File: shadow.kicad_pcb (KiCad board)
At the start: 2 copper layers, 69.8 x 78.7 mm, 100 parts, among them IC2 XB8089D, J1 USB_C_Receptacle, SW1 SW_Push, SW2 SW_Push, SW3 SW_SPST, U1 TCA9548APWR, U2 TCA9548APWR, U3 BQ24092DGQR, U4 TPS61085DGKR, U5 TPS259621DDAT

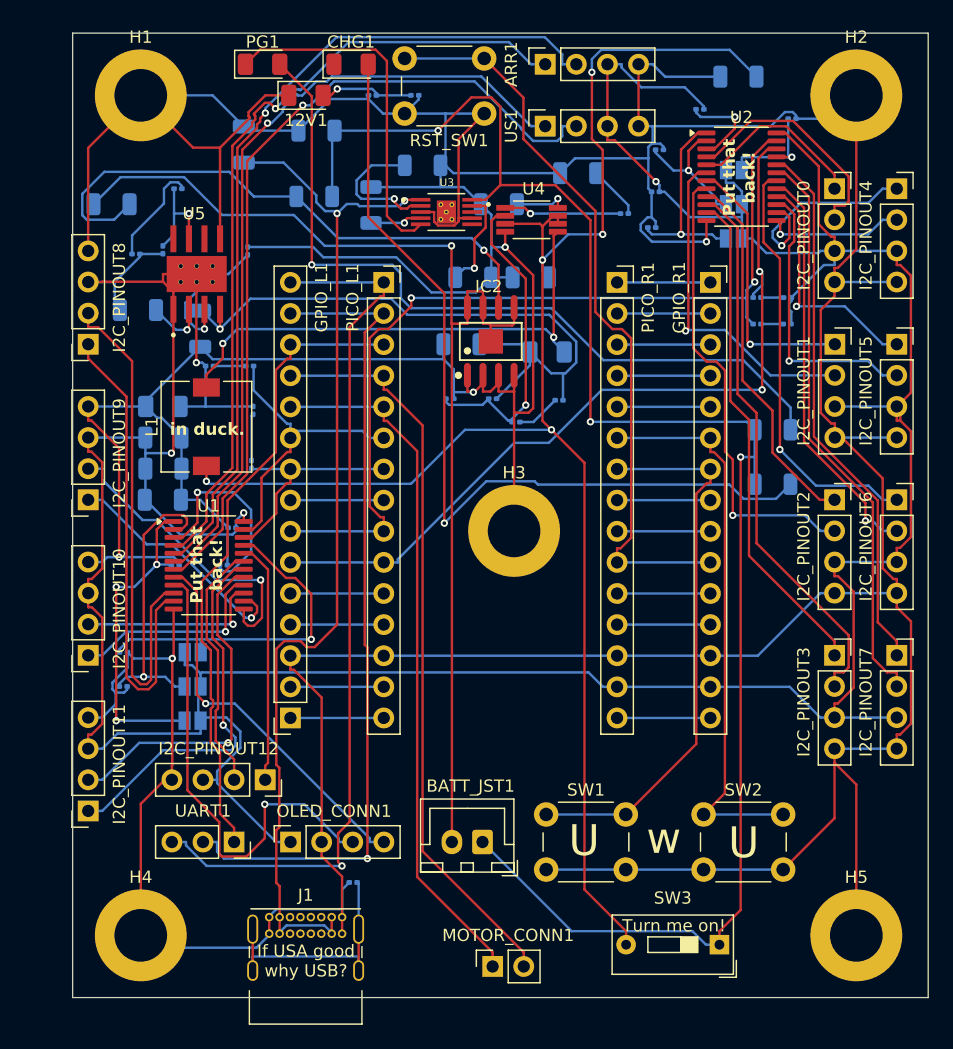
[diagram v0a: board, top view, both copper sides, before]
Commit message: Update to new cap footprint
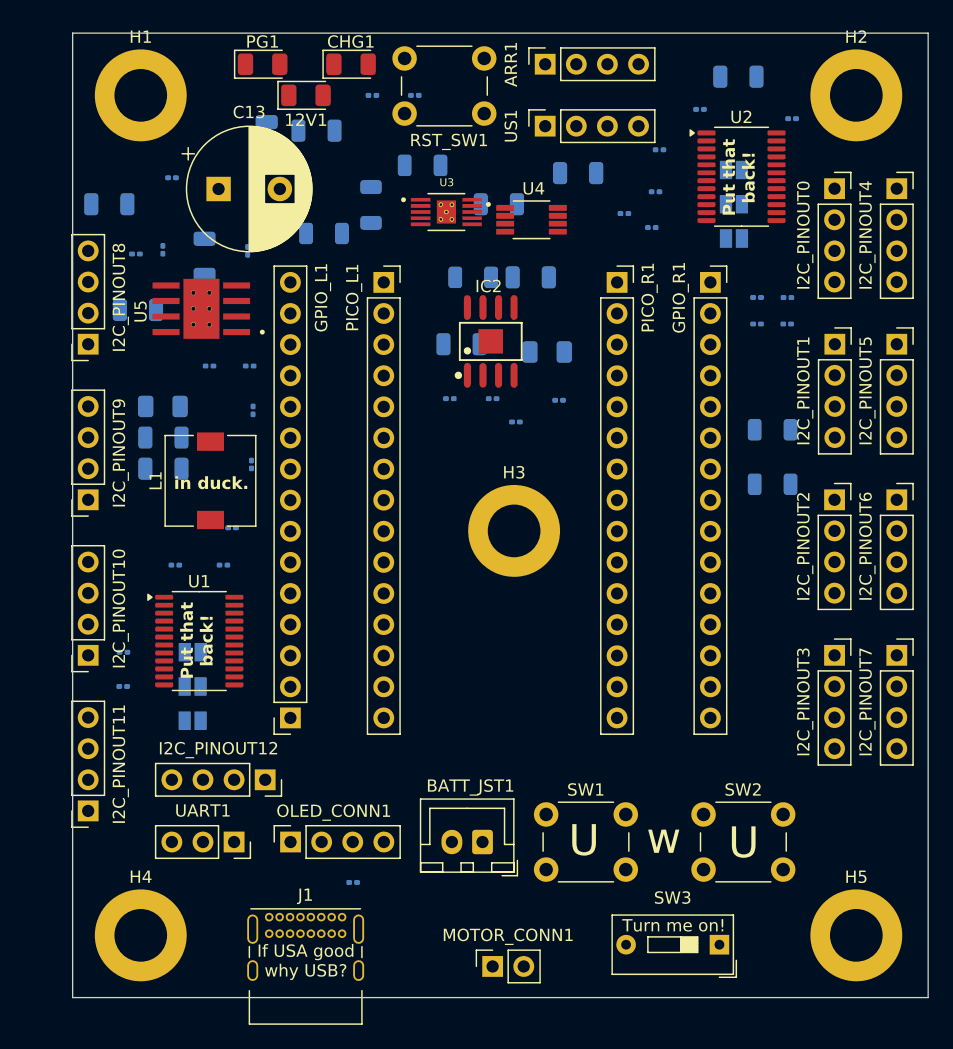
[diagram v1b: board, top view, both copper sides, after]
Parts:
- C13: footprint Capacitor_SMD:C_1206_3216Metric -> Capacitor_THT:CP_Radial_D10.0mm_P5.00mm; moved to F.Cu
- moved C13 25.8 mm to (110.5, 61.0), turned to 0 degrees
- moved U1 6.23 mm to (108.9, 97.9)
- moved C3 5.88 mm to (109.3, 66.5), turned to 90 degrees
- moved L1 4.43 mm to (109.8, 84.8)
- moved R5 3.13 mm to (119.1, 64.6)
- moved U5 2.86 mm to (109.1, 70.8), turned to 180 degrees
- moved C8 1.90 mm to (114.4, 57.0)
- moved R17 1.01 mm to (106.7, 60.1)
- moved C7 0.18 mm to (101.6, 62.2)
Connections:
- C10 pad 2: VCC -> GND
- C11 pad 1: GND -> VCC
- C11 pad 2: VCC -> GND
- C12 pad 1: GND -> VCC
- C12 pad 2: VCC -> GND
- C13 pad 1: GND -> VCC
- C13 pad 2: VCC -> GND
- D2 pad 1: GND -> VCC
- D2 pad 2: VCC -> GND
- R12 pad 1: VCC -> GND
- R13 pad 1: VCC -> GND
- R14 pad 2: GND -> VCC
- U5 pad 1: VCC -> GND
- U5 pad 5: GND -> VCC
- U5 pad 9: VCC -> GND
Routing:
- net GND: track 572.3 -> 0.00 mm, vias 5 -> 0
- net VCC: track 321.5 -> 0.00 mm, vias 4 -> 0
- net /battery/BAT+: track 137.3 -> 0.00 mm, vias 3 -> 0
- net Net-(SW3-B): track 134.9 -> 0.00 mm, vias 5 -> 0
- net /battery/BAT-: track 94.3 -> 0.00 mm, vias 1 -> 0
- net Net-(U3-IN): track 86.7 -> 0.00 mm, vias 2 -> 0
- net /GPIO8: track 73.3 -> 0.00 mm, vias 2 -> 0
- net /GPIO0: track 72.0 -> 0.00 mm, vias 1 -> 0
- net Net-(CHG1-A): track 70.8 -> 0.00 mm, vias 1 -> 0
- net /SENSOR_SCL: track 69.0 -> 0.00 mm, vias 1 -> 0
- net /US_SCL: track 68.9 -> 0.00 mm, vias 1 -> 0
- net /GPIO9: track 67.8 -> 0.00 mm, vias 2 -> 0
- net /GPIO1: track 67.3 -> 0.00 mm, vias 1 -> 0
- net /SENSOR_SDA: track 65.8 -> 0.00 mm, vias 1 -> 0
- net /US_SDA: track 65.5 -> 0.00 mm, vias 1 -> 0
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
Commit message: route traces
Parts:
- moved J1 0.94 mm to (114.6, 119.5)
- moved R30 0.77 mm to (121.6, 116.8)
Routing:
- net GND: track 0.00 -> 570.2 mm, vias 0 -> 4
- net VCC: track 0.00 -> 351.8 mm, vias 0 -> 4
- net /battery/BAT+: track 0.00 -> 138.4 mm, vias 0 -> 5
- net Net-(SW3-B): track 0.00 -> 126.4 mm, vias 0 -> 5
- net /battery/BAT-: track 0.00 -> 89.2 mm, vias 0 -> 1
- net Net-(U3-IN): track 0.00 -> 85.8 mm, vias 0 -> 2
- net /US_SCL: track 0.00 -> 82.4 mm, vias 0 -> 1
- net /SENSOR_SCL: track 0.00 -> 80.7 mm, vias 0 -> 1
- net /GPIO9: track 0.00 -> 79.0 mm, vias 0 -> 2
- net /GPIO8: track 0.00 -> 78.9 mm, vias 0 -> 2
- net /US_SDA: track 0.00 -> 78.5 mm, vias 0 -> 1
- net /SENSOR_SDA: track 0.00 -> 74.1 mm, vias 0 -> 1
- net /GPIO1: track 0.00 -> 71.4 mm, vias 0 -> 1
- net Net-(PG1-A): track 0.00 -> 70.4 mm, vias 0 -> 1
- net Net-(CHG1-A): track 0.00 -> 65.0 mm, vias 0 -> 1
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
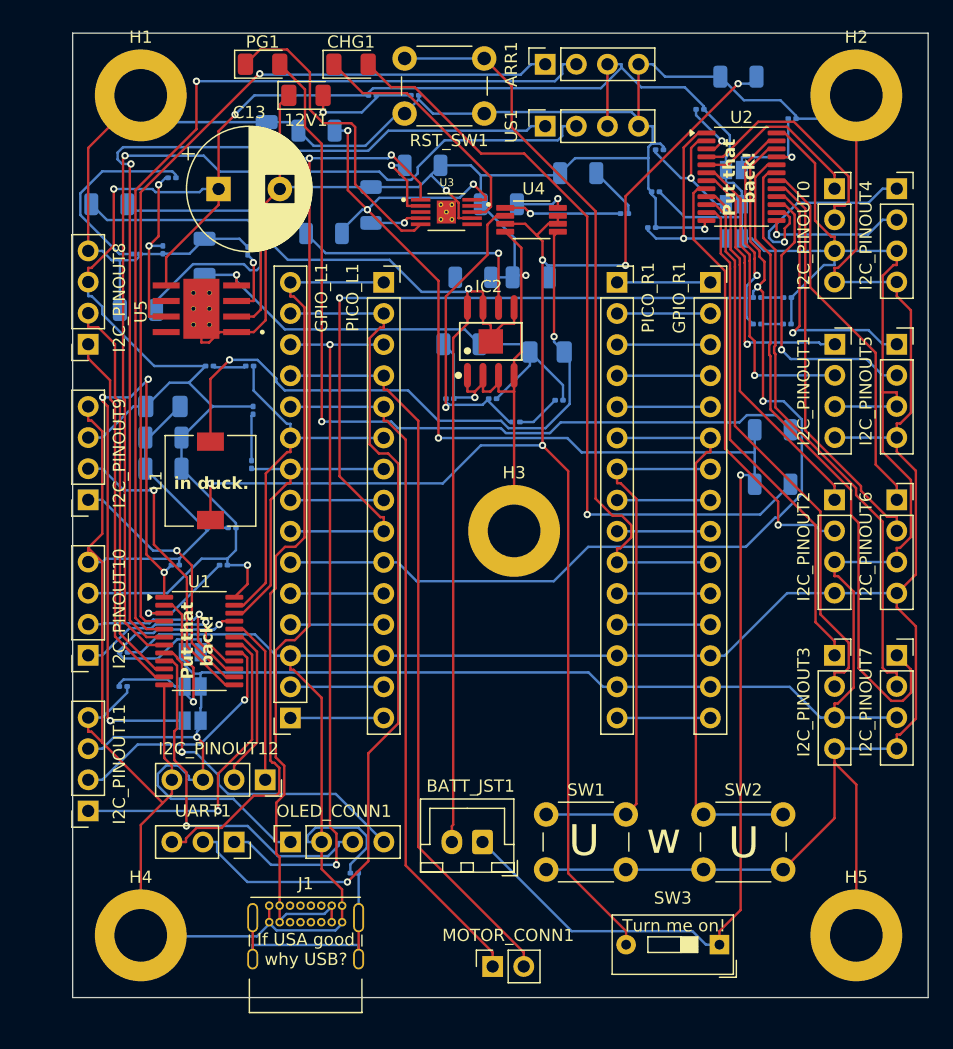
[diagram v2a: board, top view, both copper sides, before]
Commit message: fix pico mount width and orientation of left gpio
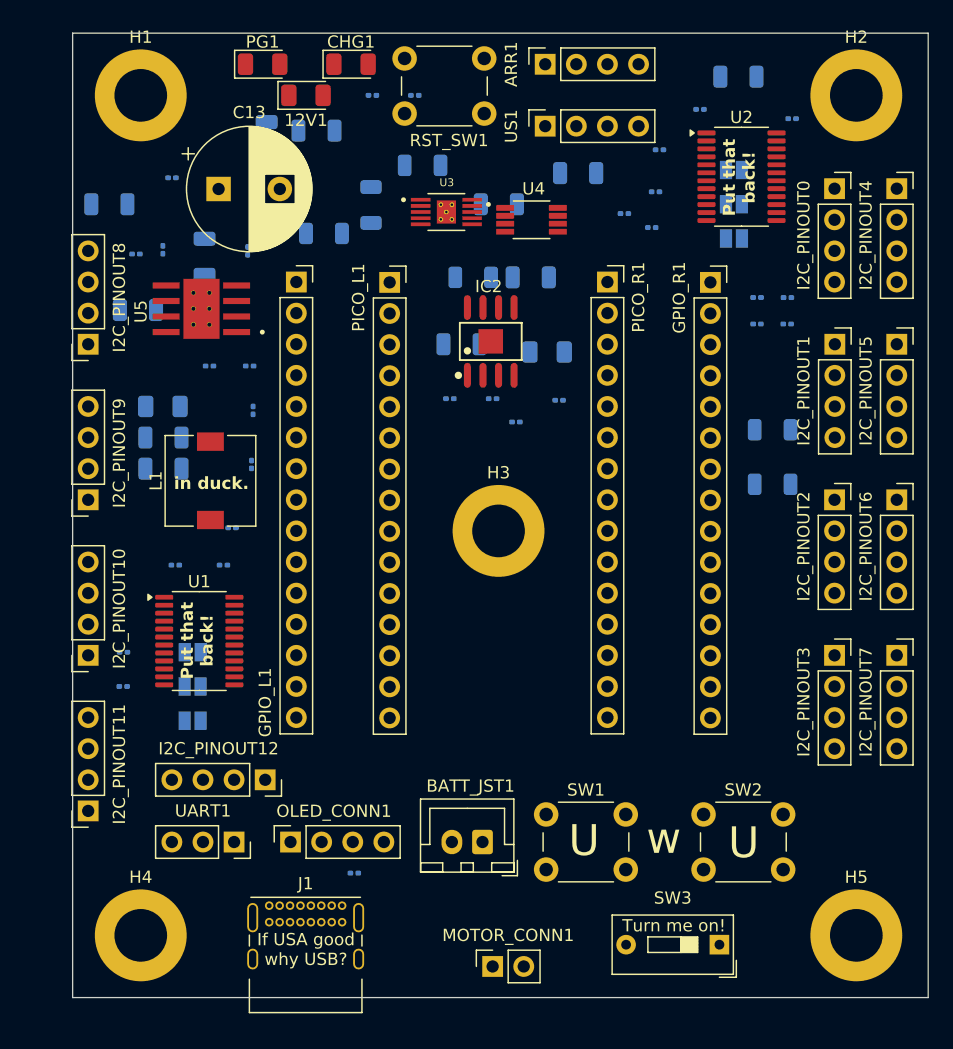
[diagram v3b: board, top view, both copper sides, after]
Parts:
- moved GPIO_L1 35.6 mm to (116.8, 68.6), turned to 0 degrees
- moved H3 1.27 mm to (133.3, 88.9)
- moved PICO_R1 0.79 mm to (142.2, 68.6)
- moved PICO_L1 0.48 mm to (124.5, 68.6)
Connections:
- GPIO_L1 pad 1: /GPIO14 -> /GPIO0
- GPIO_L1 pad 10: /GPIO5 -> /GPIO9
- GPIO_L1 pad 11: /GPIO4 -> /GPIO10
- GPIO_L1 pad 12: /GPIO3 -> /GPIO11
- GPIO_L1 pad 13: /GPIO2 -> GND
- GPIO_L1 pad 14: /GPIO1 -> /GPIO13
- GPIO_L1 pad 15: /GPIO0 -> /GPIO14
- GPIO_L1 pad 2: /GPIO13 -> /GPIO1
- GPIO_L1 pad 3: GND -> /GPIO2
- GPIO_L1 pad 4: /GPIO11 -> /GPIO3
- GPIO_L1 pad 5: /GPIO10 -> /GPIO4
- GPIO_L1 pad 6: /GPIO9 -> /GPIO5
- GPIO_L1 pad 7: /GPIO8 -> /GPIO6
- GPIO_L1 pad 9: /GPIO6 -> /GPIO8
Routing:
- net GND: track 570.2 -> 0.00 mm, vias 4 -> 0
- net VCC: track 351.8 -> 0.00 mm, vias 4 -> 0
- net /battery/BAT+: track 138.4 -> 0.00 mm, vias 5 -> 0
- net Net-(SW3-B): track 126.4 -> 0.00 mm, vias 5 -> 0
- net /battery/BAT-: track 89.2 -> 0.00 mm, vias 1 -> 0
- net Net-(U3-IN): track 85.8 -> 0.00 mm, vias 2 -> 0
- net /US_SCL: track 82.4 -> 0.00 mm, vias 1 -> 0
- net /SENSOR_SCL: track 80.7 -> 0.00 mm, vias 1 -> 0
- net /GPIO9: track 79.0 -> 0.00 mm, vias 2 -> 0
- net /GPIO8: track 78.9 -> 0.00 mm, vias 2 -> 0
- net /US_SDA: track 78.5 -> 0.00 mm, vias 1 -> 0
- net /SENSOR_SDA: track 74.1 -> 0.00 mm, vias 1 -> 0
- net /GPIO1: track 71.4 -> 0.00 mm, vias 1 -> 0
- net Net-(PG1-A): track 70.4 -> 0.00 mm, vias 1 -> 0
- net Net-(CHG1-A): track 65.0 -> 0.00 mm, vias 1 -> 0
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
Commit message: fix some stuff and retrace
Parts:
- moved R3 3.81 mm to (125.6, 78.1)
- moved 12V1 3.81 mm to (113.8, 53.3)
- moved ARR1 3.81 mm to (133.3, 50.8)
- moved BATT_JST1 3.81 mm to (128.2, 114.3)
- moved C1 3.81 mm to (136.0, 59.7)
- moved C10 3.81 mm to (100.1, 70.9)
- moved C11 3.81 mm to (102.2, 81.3)
- moved C12 3.81 mm to (102.2, 83.8)
- moved C14 3.81 mm to (107.8, 88.6)
- moved C15 3.81 mm to (142.4, 61.2)
- moved C2 3.81 mm to (129.6, 62.2)
- moved C4 3.81 mm to (126.5, 73.7)
- moved C5 3.81 mm to (149.1, 51.8)
- moved C7 3.81 mm to (97.8, 62.2)
- moved C8 3.81 mm to (110.6, 57.0)
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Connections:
- GPIO_R1 pad 1: /GPIO29 -> /GPIO15
- GPIO_R1 pad 10: /GPIO20 -> /GPIO24
- GPIO_R1 pad 11: /GPIO19 -> /GPIO25
- GPIO_R1 pad 12: /GPIO18 -> /GPIO26
- GPIO_R1 pad 13: GND -> /GPIO27
- GPIO_R1 pad 14: VCC -> /GPIO28
- GPIO_R1 pad 15: /GPIO15 -> /GPIO29
- GPIO_R1 pad 2: /GPIO28 -> VCC
- GPIO_R1 pad 3: /GPIO27 -> GND
- GPIO_R1 pad 4: /GPIO26 -> /GPIO18
- GPIO_R1 pad 5: /GPIO25 -> /GPIO19
- GPIO_R1 pad 6: /GPIO24 -> /GPIO20
- GPIO_R1 pad 7: /GPIO23 -> /GPIO21
- GPIO_R1 pad 9: /GPIO21 -> /GPIO23
- PICO_R1 pad 1: /GPIO29 -> /GPIO15
- PICO_R1 pad 10: /GPIO20 -> /GPIO24
- PICO_R1 pad 11: /GPIO19 -> /GPIO25
- PICO_R1 pad 12: /GPIO18 -> /GPIO26
- PICO_R1 pad 13: GND -> /GPIO27
- PICO_R1 pad 14: VCC -> /GPIO28
- PICO_R1 pad 15: /GPIO15 -> /GPIO29
- PICO_R1 pad 2: /GPIO28 -> VCC
- PICO_R1 pad 3: /GPIO27 -> GND
- PICO_R1 pad 4: /GPIO26 -> /GPIO18
- PICO_R1 pad 5: /GPIO25 -> /GPIO19
- PICO_R1 pad 6: /GPIO24 -> /GPIO20
- PICO_R1 pad 7: /GPIO23 -> /GPIO21
- PICO_R1 pad 9: /GPIO21 -> /GPIO23
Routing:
- net GND: track 0.00 -> 565.2 mm, vias 0 -> 2
- net VCC: track 0.00 -> 315.7 mm, vias 0 -> 5
- net /battery/BAT+: track 0.00 -> 139.7 mm, vias 0 -> 4
- net Net-(SW3-B): track 0.00 -> 132.1 mm, vias 0 -> 5
- net /US_SCL: track 0.00 -> 93.8 mm, vias 0 -> 2
- net /battery/BAT-: track 0.00 -> 92.4 mm, vias 0 -> 1
- net /US_SDA: track 0.00 -> 87.7 mm, vias 0 -> 2
- net Net-(U3-IN): track 0.00 -> 85.2 mm, vias 0 -> 2
- net /SENSOR_SCL: track 0.00 -> 82.4 mm, vias 0 -> 1
- net /SENSOR_SDA: track 0.00 -> 77.5 mm, vias 0 -> 1
- net Net-(CHG1-A): track 0.00 -> 74.8 mm, vias 0 -> 1
- net Net-(PG1-A): track 0.00 -> 74.0 mm, vias 0 -> 1
- net /GPIO9: track 0.00 -> 73.7 mm, vias 0 -> 3
- net /GPIO0: track 0.00 -> 71.7 mm, vias 0 -> 1
- net /GPIO8: track 0.00 -> 63.9 mm, vias 0 -> 1
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
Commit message: v0.0.1
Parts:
- added G***: LOGO, LOGO, F.Cu at (127.0, 96.5)
- moved H3 2.54 mm to (129.5, 86.4)
- moved BATT_JST1 1.27 mm to (128.2, 115.6)
- moved GPIO_R1 0.79 mm to (146.1, 68.6)
- moved SW1 0.76 mm to (133.4, 112.8)
- moved SW2 0.76 mm to (146.3, 112.8)
- moved SW3 0.51 mm to (147.6, 123.2)
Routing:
- net /GPIO1: track 7.63 -> 56.1 mm
- net /I2C_PINOUT2/SCL: track 0.00 -> 39.9 mm, vias 0 -> 1
- net GND: track 565.2 -> 535.6 mm, vias 2 -> 5
- net /I2C_PINOUT11/SCL: track 25.1 -> 0.00 mm, vias 1 -> 0
- net /US_SDA: track 87.7 -> 67.5 mm, vias 2 -> 4
- net /I2C_PINOUT5/SDA: track 20.1 -> 0.00 mm, vias 1 -> 0
- net VCC: track 315.7 -> 330.3 mm, vias 5 -> 1
- net /GPIO0: track 71.7 -> 57.7 mm, vias 1 -> 0
- net /I2C_PINOUT6/SDA: track 44.3 -> 33.3 mm, vias 2 -> 0
- net /I2C_PINOUT3/SCL: track 51.6 -> 40.9 mm, vias 1 -> 0
- net /battery/BAT+: track 139.7 -> 150.1 mm, vias 4 -> 3
- net /US_SCL: track 93.8 -> 83.6 mm
- net /battery/BAT-: track 92.4 -> 100.6 mm
- net /SENSOR_SDA: track 77.5 -> 69.6 mm
- net /I2C_PINOUT9/SDA: track 26.1 -> 32.6 mm, vias 1 -> 3
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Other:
- board text added: "- Cindy Shi"
- board text added: "1/25/2025"
- board text added: "Designed & Developed by: Evan Yu Logo & Backseating: Aaron Huang"
- board text added: "LOOOOOOOWWW TAAAPEERR FAAADDEEE"
- board text added: "When the bot breaks during comp but you're just a chill guy"
- board text added: "oiiaioiiiaioiiaioiiiaioiiaioiii"
- board text added: "v0.0.1 ymci.ca/shadow"

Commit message: finish pcb
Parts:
- removed R30: 0k, Resistor_SMD:R_0201_0603Metric
- C14, C15: footprint Capacitor_SMD:C_0201_0603Metric -> Capacitor_SMD:C_1206_3216Metric
- J1: footprint Connector_USB:USB_C_Receptacle_GCT_USB4085 -> USB_C:TYPE-C-SMD_20009-UCAF001-X
- R1, R11, R12, R13, R14, R15, R16, R17, R18, R19, R2, R20, R21, R22, R23, R24, R25, R26, R27, R28, R29, R3, R31, R32, R33, R34, R4: footprint Resistor_SMD:R_0201_0603Metric -> Resistor_SMD:R_1206_3216Metric
- SW3: value SW_SPST -> ~; footprint Button_Switch_THT:SW_DIP_SPSTx01_Slide_9.78x4.72mm_W7.62mm_P2.54mm -> Switch:SW-TH_K3-2235D-F1
- moved C7 25.6 mm to (123.1, 65.5)
- moved C5 22.0 mm to (130.0, 62.7)
- moved R21 12.4 mm to (99.1, 89.2), turned to -90 degrees
- moved R14 8.65 mm to (110.7, 52.1)
- moved R22 8.43 mm to (103.8, 91.9), turned to 0 degrees
- moved C15 8.24 mm to (135.3, 65.5)
- moved C2 7.21 mm to (135.8, 58.7), turned to 0 degrees
- moved R1 6.80 mm to (124.7, 82.5)
- moved R32 6.48 mm to (151.9, 78.4)
- moved R34 6.48 mm to (151.9, 76.2)
- moved C1 5.88 mm to (130.3, 58.7)
- moved R15 5.88 mm to (117.0, 51.8)
- moved R13 5.23 mm to (97.3, 61.8), turned to 90 degrees
- moved R4 4.51 mm to (135.6, 61.5)
- moved R29 4.06 mm to (149.8, 53.6)
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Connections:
- net Net-(U3-IN) renamed VBUS
- C5 pad 1: Net-(SW3-B) -> Net-(U4-EN)
- C6 pad 1: Net-(SW3-B) -> Net-(U4-EN)
- L1 pad 1: Net-(SW3-B) -> Net-(U4-EN)
- SW3 pad 2: Net-(SW3-B) -> unconnected-(SW3-Pad2)
- U4 pad 3: Net-(SW3-B) -> Net-(U4-EN)
- U4 pad 6: Net-(SW3-B) -> Net-(U4-EN)
- U4 pad 7: Net-(SW3-B) -> Net-(U4-EN)
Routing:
- net Net-(SW3-B): track 131.3 -> 0.00 mm, vias 5 -> 0
- net Net-(U4-EN): track 0.00 -> 121.9 mm, vias 0 -> 5
- net GND: track 535.6 -> 571.7 mm, vias 5 -> 3
- net /battery/BAT-: track 100.6 -> 66.6 mm
- net /I2C_PINOUT11/SCL: track 0.00 -> 25.7 mm, vias 0 -> 1
- net Net-(J1-SHIELD): track 21.4 -> 0.00 mm
- net /I2C_PINOUT5/SDA: track 0.00 -> 19.2 mm
- net /US_SDA: track 67.5 -> 83.4 mm, vias 4 -> 2
- net Net-(IC2-VDD): track 36.6 -> 21.8 mm
- net VCC: track 330.3 -> 318.8 mm, vias 1 -> 3
- net /GPIO0: track 57.7 -> 69.2 mm, vias 0 -> 1
- net /I2C_PINOUT6/SCL: track 31.0 -> 40.6 mm, vias 0 -> 3
- net /I2C_PINOUT7/SCL: track 45.8 -> 55.3 mm
- net /I2C_PINOUT1/SDA: track 25.9 -> 34.7 mm, vias 1 -> 2
- net Net-(D1-K): track 52.5 -> 44.2 mm
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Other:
- board text added: "{dblquote}what?{dblquote} - Jayson Sone"
